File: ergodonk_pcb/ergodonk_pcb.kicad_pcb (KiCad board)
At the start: 2 copper layers, 184 x 152.6 mm, 120 parts, among them J1 AudioJack4, Q1 TIP120, SW1 SW_PUSH-MX_W_LED, SW4 SW_PUSH

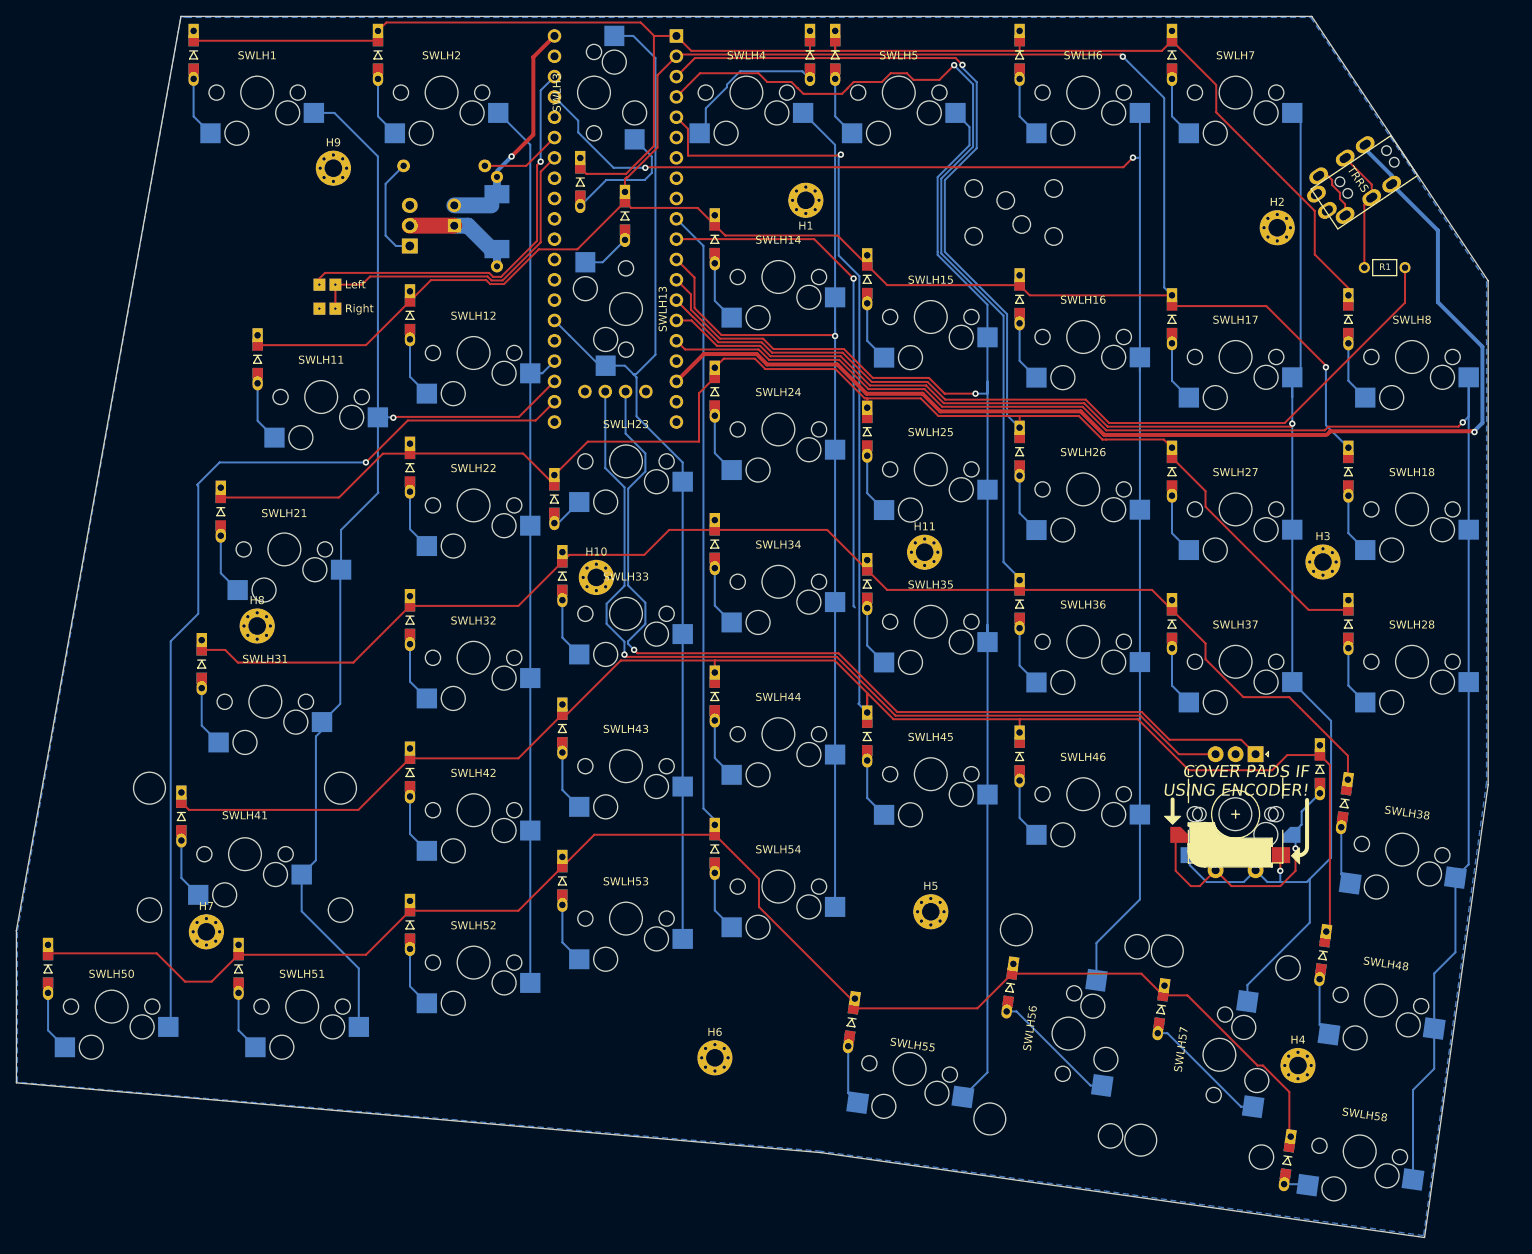
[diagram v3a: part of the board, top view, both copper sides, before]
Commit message: Created Cherry MX Doublesided mini-e footprint variant and updated schematic
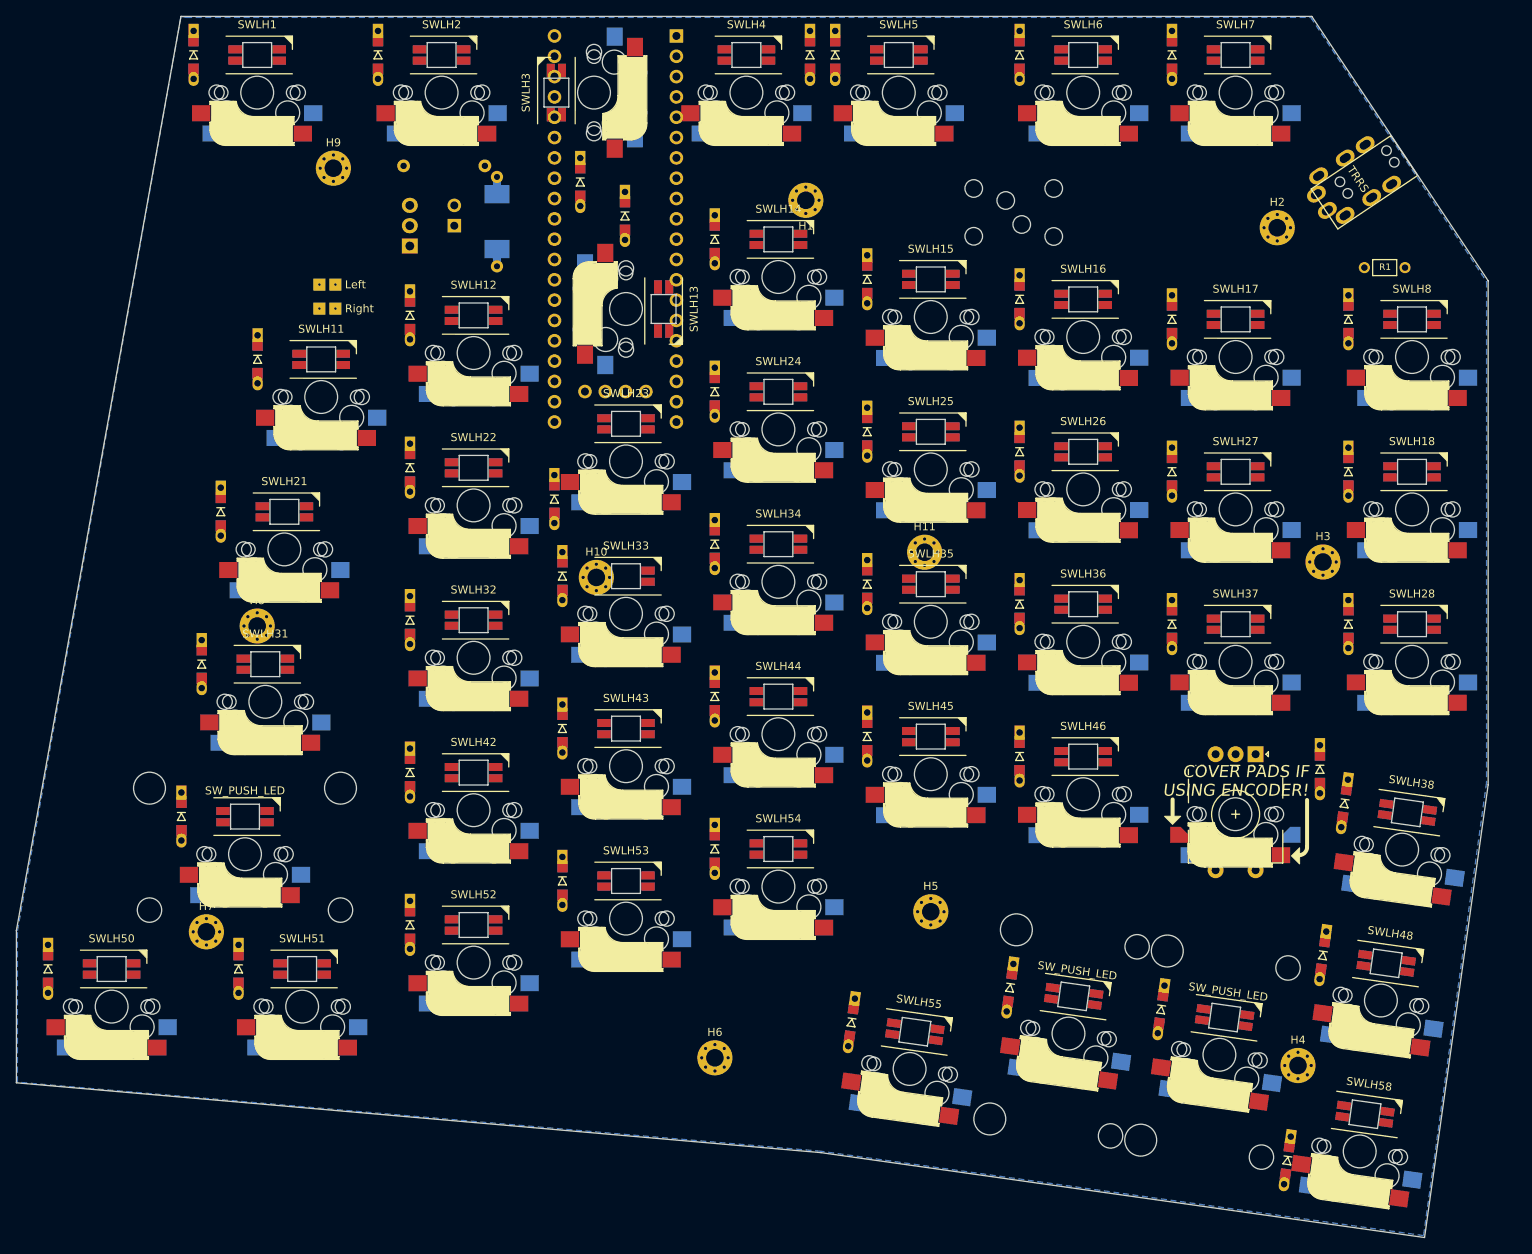
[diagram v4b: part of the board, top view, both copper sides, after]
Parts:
- SWLH1, SWLH11, SWLH12, SWLH13, SWLH14, SWLH15, SWLH16, SWLH17, SWLH18, SWLH2, SWLH22, SWLH23, SWLH24, SWLH25, SWLH26, SWLH27, SWLH28, SWLH3, SWLH32, SWLH33, SWLH34, SWLH35, SWLH36, SWLH37, SWLH38, SWLH4, SWLH42, SWLH43, SWLH44, SWLH45, SWLH46, SWLH48, SWLH5, SWLH52, SWLH53, SWLH54, SWLH58, SWLH6, SWLH7, SWLH8: value SW_PUSH -> SW_PUSH_LED; footprint ergodonk_kicad_library:CherryMX_Hotswap -> ergodonk_kicad_library:CherryMX_DoubleSided_Hotswap_miniE
- SWLH21: value SW_PUSH -> SW_PUSH_LED; footprint ergodonk_kicad_library:CherryMX_Hotswap_1.5u -> ergodonk_kicad_library:CherryMX_DoubleSided_Hotswap_miniE_1.5u
- SWLH31: value SW_PUSH -> SW_PUSH_LED; footprint ergodonk_kicad_library:CherryMX_Hotswap_1.75u_ergodonk -> ergodonk_kicad_library:CherryMX_DoubleSided_Hotswap_miniE_1.75u
- SWLH41: value SW_PUSH -> SW_PUSH_LED; footprint ergodonk_kicad_library:CherryMX_Hotswap_2u_ergodonk_Stabs -> ergodonk_kicad_library:CherryMX_DoubleSided_Hotswap_miniE_2u
- SWLH50, SWLH51: value SW_PUSH -> SW_PUSH_LED; footprint ergodonk_kicad_library:CherryMX_Hotswap_1.25u_ergodonk -> ergodonk_kicad_library:CherryMX_DoubleSided_Hotswap_miniE_1.25u
- SWLH55: value SW_PUSH -> SW_PUSH_LED; footprint ergodonk_kicad_library:CherryMX_Hotswap_1.25u_Vert_ergodonk -> ergodonk_kicad_library:CherryMX_DoubleSided_Hotswap_miniE_1.25u_Vertical
- SWLH56, SWLH57: value SW_PUSH -> SW_PUSH_LED; footprint ergodonk_kicad_library:CherryMX_Hotswap_2u_ergodonk_Stabs -> ergodonk_kicad_library:CherryMX_DoubleSided_Hotswap_miniE_2u_Vertical
- turned SWLH1 to 0 degrees
- turned SWLH11 to 0 degrees
- turned SWLH12 to 0 degrees
- turned SWLH13 to -90 degrees
- turned SWLH14 to 0 degrees
- turned SWLH15 to 0 degrees
- turned SWLH16 to 0 degrees
- turned SWLH17 to 0 degrees
- turned SWLH18 to 0 degrees
- turned SWLH2 to 0 degrees
- turned SWLH21 to 0 degrees
- turned SWLH22 to 0 degrees
- turned SWLH23 to 0 degrees
- turned SWLH24 to 0 degrees
- turned SWLH25 to 0 degrees
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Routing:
- net row4: track 289.2 -> 0.00 mm, vias 1 -> 0
- net row3: track 276.9 -> 0.00 mm, vias 1 -> 0
- net row5: track 270.1 -> 0.00 mm
- net row1: track 268.9 -> 0.00 mm, vias 2 -> 0
- net row2: track 266.2 -> 0.00 mm, vias 1 -> 0
- net SW47A: track 225.4 -> 0.00 mm, vias 2 -> 0
- net col8: track 212.4 -> 0.00 mm, vias 1 -> 0
- net row0: track 196.7 -> 0.00 mm
- net col6: track 190.7 -> 0.00 mm, vias 2 -> 0
- net col5: track 178.8 -> 0.00 mm, vias 1 -> 0
- net col1: track 150.4 -> 0.00 mm, vias 1 -> 0
- net TRRS_VCC: track 148.1 -> 0.00 mm, vias 1 -> 0
- net col3: track 132.9 -> 0.00 mm
- net col4: track 131.8 -> 0.00 mm, vias 1 -> 0
- net encA: track 119.4 -> 0.00 mm, vias 1 -> 0
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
